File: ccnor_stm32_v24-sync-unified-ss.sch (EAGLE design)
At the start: 148 parts, among them J1 M02PT, J2 M021P25, J3 M02XH, J4 M021P25, Q1 2N7002P, Q2 WSP4406, Q3 WSP4406, Q4 NCE3018AS, Q5 IRLB8314PBF, Q6 2302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

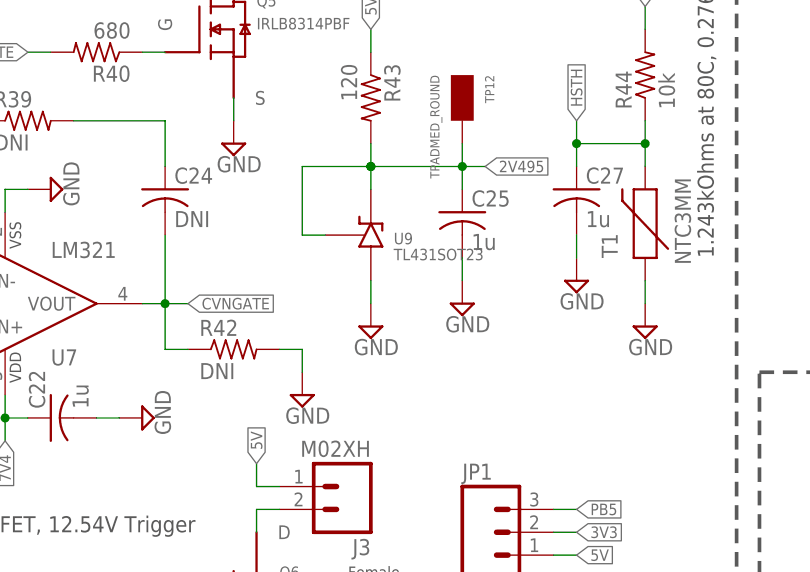
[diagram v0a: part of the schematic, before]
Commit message: Added TL431 through-hole, fixed DRC errors
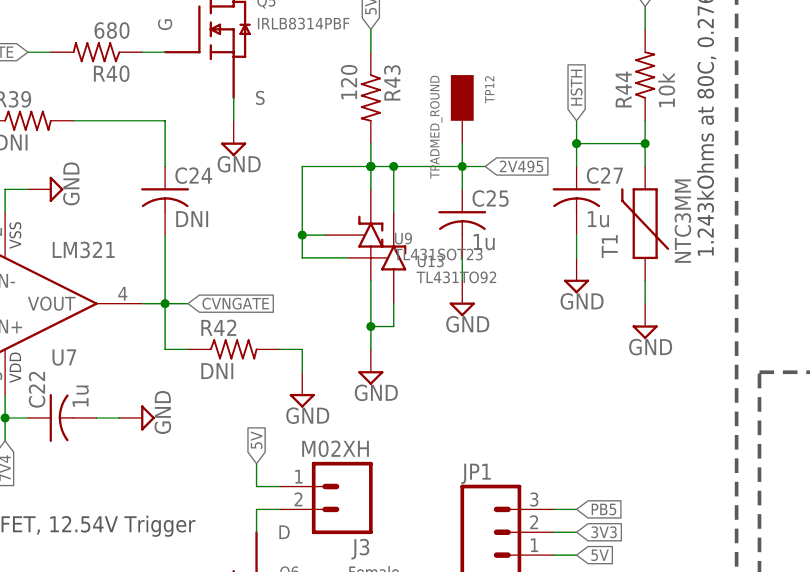
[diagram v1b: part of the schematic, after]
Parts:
- added U13: TL431TO92, custom:TL431TO92
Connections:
- net 2V495: now also U13.K, U13.REF
- net GND: now also U13.A
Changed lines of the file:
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@@
 <part name="C32" library="resistor" deviceset="CPOL-US" device="E2.5-7" value="470u"/>
 <part name="C35" library="resistor" deviceset="CPOL-US" device="E2.5-7" value="470u"/>
+<part name="U13" library="custom" deviceset="TL431" device="TO92"/>
 </parts>
 <sheets>
@@
 <instance part="SUPPLY21" gate="GND" x="215.9" y="109.22"/>
 <instance part="U9" gate="U1" x="205.74" y="116.84"/>
-<instance part="SUPPLY22" gate="GND" x="205.74" y="106.68"/>
+<instance part="SUPPLY22" gate="GND" x="205.74" y="101.6"/>
 <instance part="SUPPLY2" gate="GND" x="76.2" y="20.32"/>
 <instance part="J1" gate="J1" x="-10.16" y="149.86"/>
@@
 <instance part="C32" gate="G$1" x="292.1" y="22.86"/>
 <instance part="C35" gate="G$1" x="340.36" y="22.86"/>
+<instance part="U13" gate="U1" x="208.28" y="114.3"/>
 </instances>
 <busses>
@@
 <pinref part="U9" gate="U1" pin="A"/>
 <pinref part="SUPPLY22" gate="GND" pin="GND"/>
-<wire x1="205.74" y1="109.22" x2="205.74" y2="111.76" width="0.1524" layer="91"/>
+<wire x1="205.74" y1="104.14" x2="205.74" y2="106.68" width="0.1524" layer="91"/>
+<pinref part="U13" gate="U1" pin="A"/>
+<wire x1="205.74" y1="106.68" x2="205.74" y2="111.76" width="0.1524" layer="91"/>
+<wire x1="205.74" y1="106.68" x2="208.28" y2="106.68" width="0.1524" layer="91"/>
+<wire x1="208.28" y1="106.68" x2="208.28" y2="109.22" width="0.1524" layer="91"/>
+<junction x="205.74" y="106.68"/>
 </segment>
 <segment>
@@
 <junction x="205.74" y="124.46"/>
 <pinref part="C25" gate="G$1" pin="1"/>
-<wire x1="205.74" y1="124.46" x2="215.9" y2="124.46" width="0.1524" layer="91"/>
+<wire x1="205.74" y1="124.46" x2="208.28" y2="124.46" width="0.1524" layer="91"/>
+<wire x1="208.28" y1="124.46" x2="215.9" y2="124.46" width="0.1524" layer="91"/>
 <wire x1="215.9" y1="124.46" x2="215.9" y2="121.92" width="0.1524" layer="91"/>
 <wire x1="215.9" y1="124.46" x2="218.44" y2="124.46" width="0.1524" layer="91"/>
@@
 <pinref part="TP12" gate="TP1" pin="1"/>
 <wire x1="215.9" y1="127" x2="215.9" y2="124.46" width="0.1524" layer="91"/>
-</segment>
-<segment>
+<pinref part="U13" gate="U1" pin="K"/>
+<wire x1="208.28" y1="119.38" x2="208.28" y2="124.46" width="0.1524" layer="91"/>
+<pinref part="U13" gate="U1" pin="REF"/>
+<wire x1="203.2" y1="114.3" x2="198.12" y2="114.3" width="0.1524" layer="91"/>
+<wire x1="198.12" y1="114.3" x2="198.12" y2="116.84" width="0.1524" layer="91"/>
+<junction x="198.12" y="116.84"/>
+<junction x="208.28" y="124.46"/>
+</segment>
+<segment>
